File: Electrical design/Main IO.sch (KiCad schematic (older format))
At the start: 98 parts

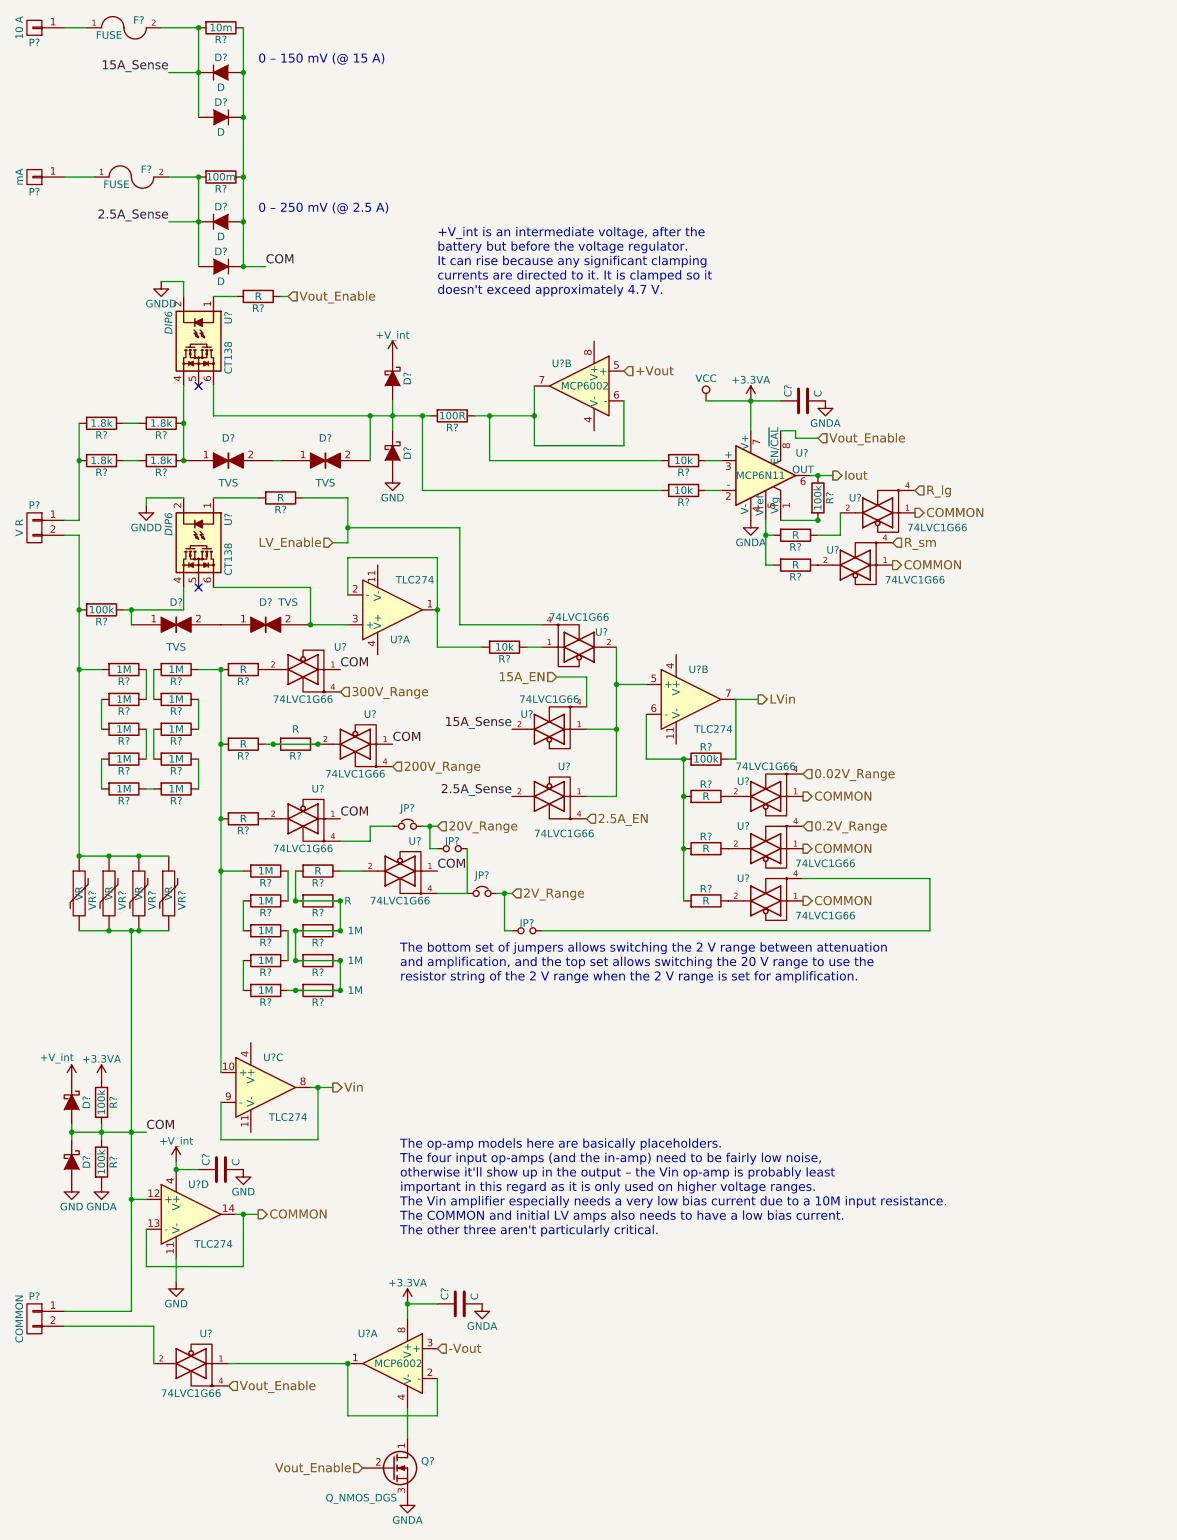
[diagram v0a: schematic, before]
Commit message: Updated schematics.
Added speaker / buzzer, reset circuit (battery under-voltage lockout), changed battery charger IC.
Altered Vout circuit.
Added most resistor / capacitor values (those missing are either dependent on battery thermistor or ADC).
Updated to show "correct" op-amps.
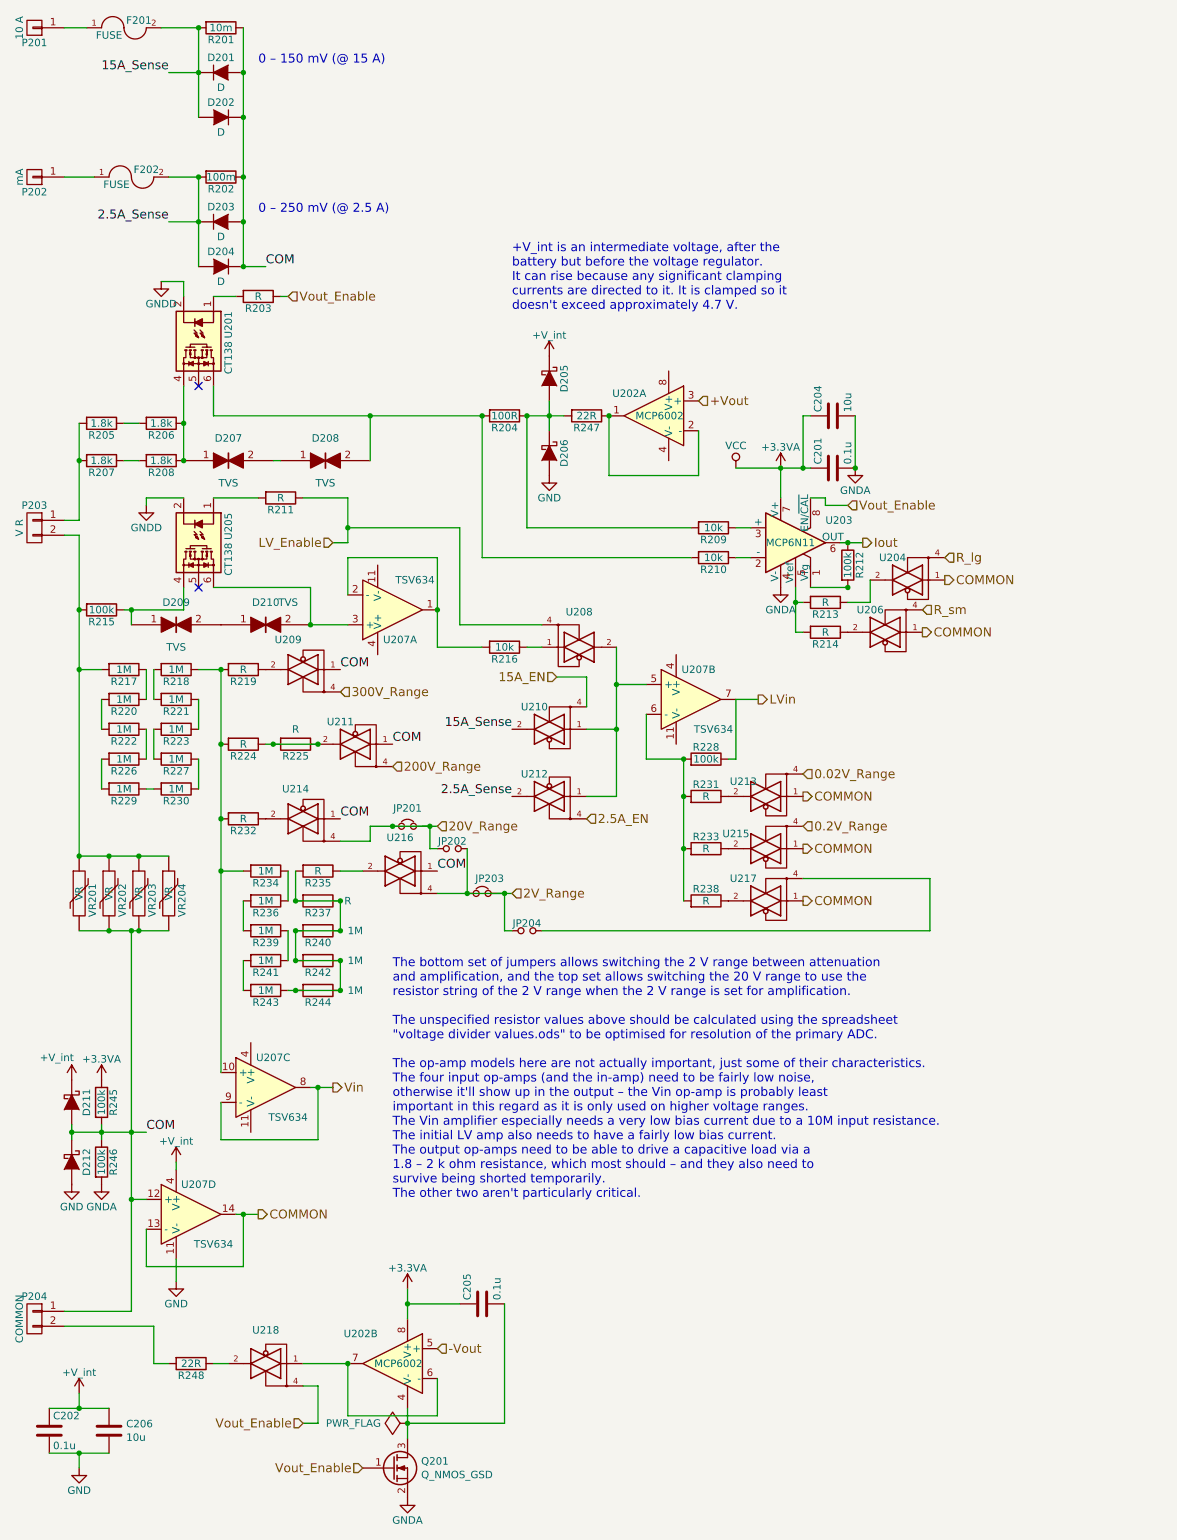
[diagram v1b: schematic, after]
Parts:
- removed C?: C, symbol C
- removed Q?: Q_NMOS_DGS, symbol Q_NMOS_DGS
- removed U? (x13): 74LVC1G66, symbol 74LVC1G66
- added C204, C206: 10u, my footprints:SMDuniversal_0603to1210_HandSoldering, symbol C
- added C205: 0.1u, my footprints:SMDuniversal_0603to1210_HandSoldering, symbol C
- added Q201: Q_NMOS_GSD, TO_SOT_Packages_SMD:SOT-23, symbol Q_NMOS_GSD
- added R247, R248: 22R, my footprints:SMDuniversal_0603to1210_HandSoldering, symbol R
- added U204, U206, U208, U209, U210, U211, U212, U213, U214, U215, U216, U217, U218: 74LVC1G66 GNDA, TO_SOT_Packages_SMD:SOT-353, symbol 74LVC1G66_GNDA
- C201, C202: renamed from C?; value C -> 0.1u; footprint (none) -> my footprints:SMDuniversal_0603to1210_HandSoldering
- D201, D202, D203, D204: renamed from D?; footprint (none) -> my footprints:Diode_R-6_Horizontal_RM15
- D205, D206, D211, D212: renamed from D?; footprint (none) -> my footprints:SC-90A
- D207, D208, D209, D210: renamed from D?; footprint (none) -> Diodes_SMD:SMB_Handsoldering
- F201, F202: renamed from F?; footprint (none) -> my footprints:Fuseholder6x32_horiz_open_inline_Type-I
- JP201, JP202, JP203, JP204: renamed from JP?; footprint (none) -> Resistors_SMD:R_0603_HandSoldering
- P201, P202: renamed from P?; footprint (none) -> Connect:Banana_Jack_1Pin
- P203, P204: renamed from P?; footprint (none) -> my footprints:Banana_Jack_1Pin_2Contact_SM_Top
- R201, R202: renamed from R?; footprint (none) -> Resistors_Universal:Resistor_SMD+THTuniversal_0805to2512_RM10_HandSoldering
- R203, R204, R209, R210, R211, R212, R213, R214, R216, R217, R218, R219, R220, R221, R222, R223, R224, R225, R226, R227, R228, R229, R230, R231, R232, R233, R234, R235, R236, R237, R238, R239, R240, R241, R242, R243, R244, R245, R246: renamed from R?; footprint (none) -> my footprints:SMDuniversal_0603to1210_HandSoldering
- R205, R206, R207, R208: renamed from R?; footprint (none) -> Resistors_Universal:Resistor_SMDuniversal_0805to2512_HandSoldering
- R215: renamed from R?; footprint (none) -> Resistors_ThroughHole:Resistor_Horizontal_RM20mm
- U201, U205: renamed from U?; footprint DIP6 -> Housings_DIP:DIP-6_W7.62mm_LongPads
- U202: renamed from U?; footprint (none) -> my footprints:MSOP-8_3x3mm_Pitch0.65mm
- U203: renamed from U?; footprint (none) -> Housings_SOIC:SOIC-8_3.9x4.9mm_Pitch1.27mm
- U207: renamed from U?; value TLC274 -> TSV634; footprint (none) -> my footprints:TSSOP-14_4.4x5mm_Pitch0.65mm
- VR201, VR202, VR203, VR204: renamed from VR?; footprint (none) -> Varistors:RV_Disc_D15.5_W5.4_P7.5
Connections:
- net +3.3VA: now also C204.1, C205.1, U204.5 (VCC), U206.5 (VCC), U208.5 (VCC), U209.5 (VCC), U210.5 (VCC), U211.5 (VCC), U212.5 (VCC), U213.5 (VCC), U214.5 (VCC), U215.5 (VCC), U216.5 (VCC), U217.5 (VCC), U218.5 (VCC)
- net +V_int: now also C206.2
- net +Vout: now also U202.3 (+); no longer U202.5 (+)
- net -Vout: now also U202.5 (+); no longer U202.3 (+)
- net 0.02V_Range: now also U213.4
- net 0.2V_Range: now also U215.4
- net 15A_EN: now also U210.4
- net 15A_Sense: now also U210.2
- net 2.5A_EN: now also U212.4
- net 2.5A_Sense: now also U212.2
- net 200V_Range: now also U211.4
- net 20V_Range: now also JP201.1, U214.4
- net 2V_Range: now also JP202.2, JP203.1, U216.4
- net 300V_Range: now also U209.4
- net COM: now also U209.1, U211.1, U214.1, U216.1
- net COMMON: now also U204.1, U206.1, U213.1, U215.1, U217.1
- net GND: now also C206.1
- net GNDA: now also C204.2, Q201.2 (S), U204.3 (GNDA), U206.3 (GNDA), U208.3 (GNDA), U209.3 (GNDA), U210.3 (GNDA), U211.3 (GNDA), U212.3 (GNDA), U213.3 (GNDA), U214.3 (GNDA), U215.3 (GNDA), U216.3 (GNDA), U217.3 (GNDA), U218.3 (GNDA)
- net LV_Enable: now also U208.4
- net R_lg: now also U204.4
- net R_sm: now also U206.4
- net Vout_Enable: now also Q201.1 (G), U218.4
- net at R224.1, R225.1, R225.2: now also U211.2
- net at R232.1: now also U214.2
- net at R219.1: now also U209.2
- net at R204.1, R209.2: now also D205.2 (A), D206.1 (K), R247.2; no longer U202.6 (-), U202.7
- net at D208.2, R204.2, R210.2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: no longer D205.2 (A), D206.1 (K)
- net at R235.1: now also U216.2
- net at U207.5 (+): now also U208.2, U210.1, U212.1
- net at R233.1: now also U215.2
- net at R231.1: now also U213.2
- net at R213.1: now also U204.2
- net at R214.1: now also U206.2
- net at R216.1: now also U208.1
- net at P204.2 (P2): now also R248.2
- net at U202.4 (V-): now also C205.2, Q201.3 (D)
- net at JP204.2: now also U217.4
- net at R238.1: now also U217.2
- new net: U202.6 (-), U202.7, U218.1
- new net: R247.1, U202.1, U202.2 (-)
- new net: R248.1, U218.2
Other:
- note added: "The bottom set of jumpers allows switching the 2 V range between attenuation\nand amplification, and the top set allows switching the 20 V range to use the\nresistor string of the 2 V range when the 2 V range is set for amplification.\n\nThe unspecified resistor values above should be calculated using the spreadsheet\n"voltage divider values.ods" to be optimised for resolution of the primary ADC.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"
- note removed: "The bottom set of jumpers allows switching the 2 V range between attenuation\nand amplification, and the top set allows switching the 20 V range to use the\nresistor string of the 2 V range when the 2 V range is set for amplification."
- note removed: "The op-amp models here are basically placeholders.\nThe four input op-amps (and the in-amp) need to be fairly low noise,\notherwise it'll show up in the output – the Vin op-amp is probably least\nimportant in this regard as it is only used on higher voltage ranges.\nThe Vin amplifier especially needs a very low bias current due to a 10M input resistance.\nThe COMMON and initial LV amps also needs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"
- moved on the sheet: C201, C202, D205, D206, R204, R209, R210, R212, R213, R214, U203

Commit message: Update External Design. Add battery sense capacitor. Update footprints.
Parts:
- C201, C202, C205: footprint my footprints:SMDuniversal_0603to1210_HandSoldering -> my footprints:SMDuniversal_0603to0805_HandSoldering
- C204, C206: footprint my footprints:SMDuniversal_0603to1210_HandSoldering -> my footprints:SMDuniversal_0603to1206_HandSoldering
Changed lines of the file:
@@
 Sheet 2 5
 Title "Main I/O"
-Date ""
-Rev ""
+Date "2016-06-22"
+Rev "0.5"
 Comp ""
 Comment1 ""
@@
 F 0 "C202" H 825 10150 50  0000 L CNN
 F 1 "0.1u" H 825 9950 50  0000 L CNN
-F 2 "my footprints:SMDuniversal_0603to1210_HandSoldering" H 838 9900 50  0001 C CNN
+F 2 "my footprints:SMDuniversal_0603to0805_HandSoldering" H 838 9900 50  0001 C CNN
 F 3 "" H 800 10050 50  0000 C CNN
 	1    800  10050
@@
 F 0 "C201" H 6075 3700 50  0000 L CNN
 F 1 "0.1u" H 6075 3500 50  0000 L CNN
-F 2 "my footprints:SMDuniversal_0603to1210_HandSoldering" H 6088 3450 50  0001 C CNN
+F 2 "my footprints:SMDuniversal_0603to0805_HandSoldering" H 6088 3450 50  0001 C CNN
 F 3 "" H 6050 3600 50  0000 C CNN
 	1    6050 3600
@@
 F 0 "C206" H 1085 10004 50  0000 R CNN
 F 1 "10u" H 1085 10095 50  0000 R CNN
-F 2 "my footprints:SMDuniversal_0603to1210_HandSoldering" H 1238 9900 50  0001 C CNN
+F 2 "my footprints:SMDuniversal_0603to1206_HandSoldering" H 1238 9900 50  0001 C CNN
 F 3 "" H 1200 10050 50  0000 C CNN
 	1    1200 10050
@@
 F 0 "C205" H 3725 9300 50  0000 L CNN
 F 1 "0.1u" H 3725 9100 50  0000 L CNN
-F 2 "my footprints:SMDuniversal_0603to1210_HandSoldering" H 3738 9050 50  0001 C CNN
+F 2 "my footprints:SMDuniversal_0603to0805_HandSoldering" H 3738 9050 50  0001 C CNN
 F 3 "" H 3700 9200 50  0000 C CNN
 	1    3700 9200
@@
 F 0 "C204" H 6075 3350 50  0000 L CNN
 F 1 "10u" H 6075 3150 50  0000 L CNN
-F 2 "my footprints:SMDuniversal_0603to1210_HandSoldering" H 6088 3100 50  0001 C CNN
+F 2 "my footprints:SMDuniversal_0603to1206_HandSoldering" H 6088 3100 50  0001 C CNN
 F 3 "" H 6050 3250 50  0000 C CNN
 	1    6050 3250
